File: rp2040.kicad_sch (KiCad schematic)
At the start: 15 parts, among them U3 RP2040

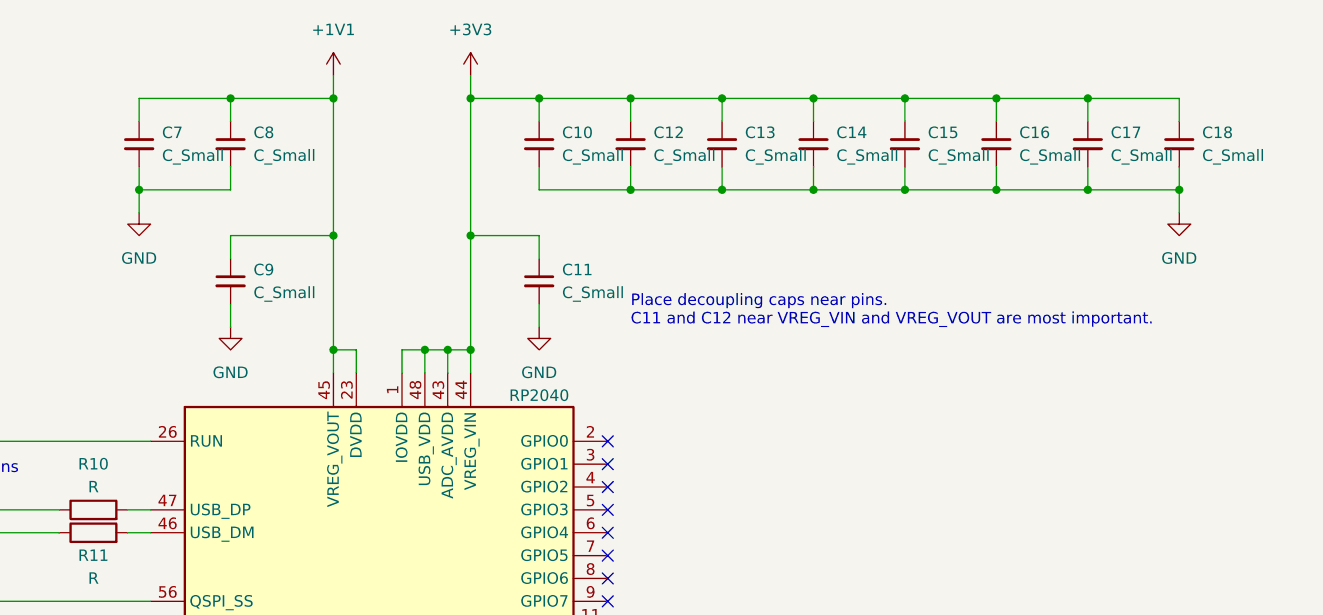
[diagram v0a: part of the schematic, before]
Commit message: Complete power regulator schematics
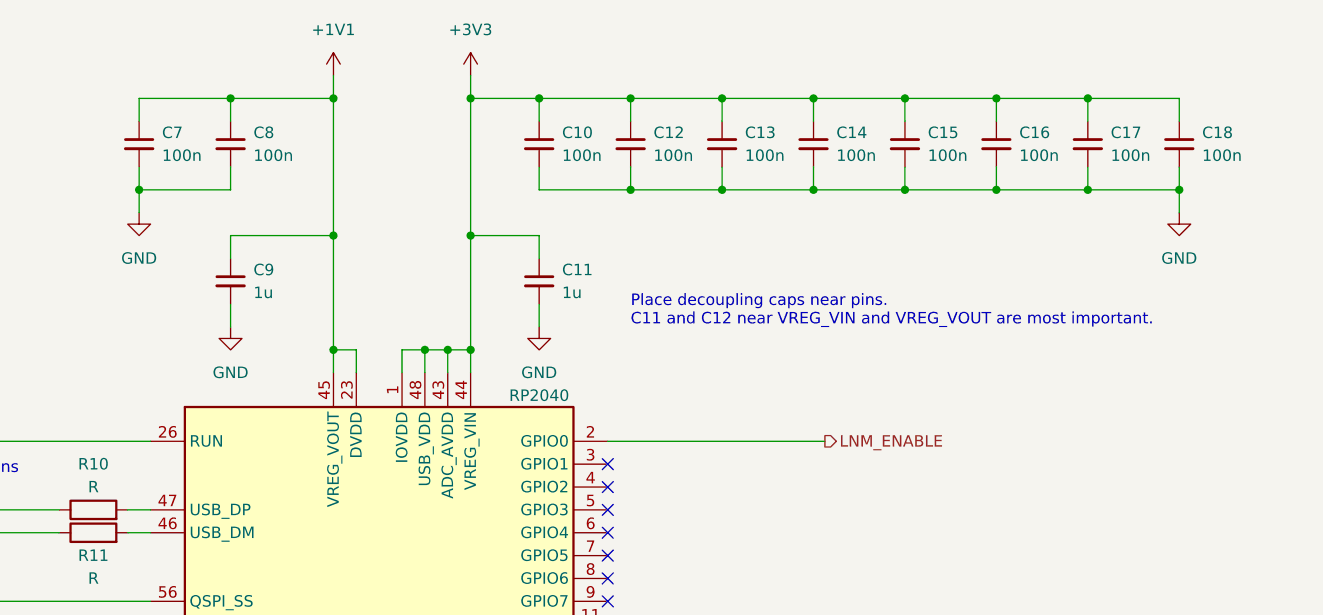
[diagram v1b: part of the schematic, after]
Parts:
- C10, C12, C13, C14, C15, C16, C17, C18, C7, C8: value C_Small -> 100n
- C11, C9: value C_Small -> 1u
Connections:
- net LNM_ENABLE: now reaches U3.2 (GPIO0)
- no-connect marks 30 -> 29
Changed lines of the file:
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@@
 		(at 166.37 115.57)
-	)
-	(no_connect
-		(at 166.37 72.39)
 	)
 	(bus_entry
@@
 		(pts
 			(xy 146.05 62.23) (xy 148.59 62.23)
+		)
+		(stroke
+			(width 0)
+			(type default)
+		)
+	)
+	(wire
+		(pts
+			(xy 166.37 72.39) (xy 190.5 72.39)
 		)
 		(stroke
@@
 			)
 			(justify right)
+		)
+	)
+	(hierarchical_label "LNM_ENABLE"
+		(shape output)
+		(at 190.5 72.39 0)
+		(fields_autoplaced yes)
+		(effects
+			(font
+				(size 1.27 1.27)
+			)
+			(justify left)
 		)
 	)
@@
 		(fields_autoplaced yes)
 		(property "Reference" "C13"
-			(at 181.61 38.1063 0)
+			(at 181.61 38.1062 0)
 			(effects
 				(font
@@
 			)
 		)
-		(property "Value" "C_Small"
-			(at 181.61 40.6463 0)
+		(property "Value" "100n"
+			(at 181.61 40.6462 0)
 			(effects
 				(font
@@
 		(fields_autoplaced yes)
 		(property "Reference" "C16"
-			(at 212.09 38.1063 0)
+			(at 212.09 38.1062 0)
 			(effects
 				(font
@@
 			)
 		)
-		(property "Value" "C_Small"
-			(at 212.09 40.6463 0)
+		(property "Value" "100n"
+			(at 212.09 40.6462 0)
 			(effects
 				(font
@@
 		(fields_autoplaced yes)
 		(property "Reference" "C14"
-			(at 191.77 38.1063 0)
+			(at 191.77 38.1062 0)
 			(effects
 				(font
@@
 			)
 		)
-		(property "Value" "C_Small"
-			(at 191.77 40.6463 0)
+		(property "Value" "100n"
+			(at 191.77 40.6462 0)
 			(effects
 				(font
@@
 		(fields_autoplaced yes)
 		(property "Reference" "C9"
-			(at 127 53.3463 0)
+			(at 127 53.3462 0)
 			(effects
 				(font
@@
 			)
 		)
-		(property "Value" "C_Small"
-			(at 127 55.8863 0)
+		(property "Value" "1u"
+			(at 127 55.8862 0)
 			(effects
 				(font
@@
 		(fields_autoplaced yes)
 		(property "Reference" "C7"
-			(at 116.84 38.1063 0)
+			(at 116.84 38.1062 0)
 			(effects
 				(font
@@
 			)
 		)
-		(property "Value" "C_Small"
-			(at 116.84 40.6463 0)
+		(property "Value" "100n"
+			(at 116.84 40.6462 0)
 			(effects
 				(font
@@
 		(fields_autoplaced yes)
 		(property "Reference" "C12"
-			(at 171.45 38.1063 0)
+			(at 171.45 38.1062 0)
 			(effects
 				(font
@@
 			)
 		)
-		(property "Value" "C_Small"
-			(at 171.45 40.6463 0)
+		(property "Value" "100n"
+			(at 171.45 40.6462 0)
 			(effects
 				(font
@@
 		(fields_autoplaced yes)
 		(property "Reference" "C11"
-			(at 161.29 53.3463 0)
+			(at 161.29 53.3462 0)
 			(effects
 				(font
@@
 			)
 		)
-		(property "Value" "C_Small"
-			(at 161.29 55.8863 0)
+		(property "Value" "1u"
+			(at 161.29 55.8862 0)
 			(effects
 				(font
@@
 		(fields_autoplaced yes)
 		(property "Reference" "C10"
-			(at 161.29 38.1063 0)
+			(at 161.29 38.1062 0)
 			(effects
 				(font
@@
 			)
 		)
-		(property "Value" "C_Small"
-			(at 161.29 40.6463 0)
+		(property "Value" "100n"
+			(at 161.29 40.6462 0)
 			(effects
 				(font
@@
 		(fields_autoplaced yes)
 		(property "Reference" "C17"
-			(at 222.25 38.1063 0)
+			(at 222.25 38.1062 0)
 			(effects
 				(font
@@
 			)
 		)
-		(property "Value" "C_Small"
-			(at 222.25 40.6463 0)
+		(property "Value" "100n"
+			(at 222.25 40.6462 0)
 			(effects
 				(font
@@
 		(fields_autoplaced yes)
 		(property "Reference" "C15"
-			(at 201.93 38.1063 0)
+			(at 201.93 38.1062 0)
 			(effects
 				(font
@@
 			)
 		)
-		(property "Value" "C_Small"
-			(at 201.93 40.6463 0)
+		(property "Value" "100n"
+			(at 201.93 40.6462 0)
 			(effects
 				(font
@@
 		(fields_autoplaced yes)
 		(property "Reference" "C18"
-			(at 232.41 38.1063 0)
+			(at 232.41 38.1062 0)
 			(effects
 				(font
@@
 			)
 		)
-		(property "Value" "C_Small"
-			(at 232.41 40.6463 0)
+		(property "Value" "100n"
+			(at 232.41 40.6462 0)
 			(effects
 				(font
@@
 		(fields_autoplaced yes)
 		(property "Reference" "C8"
-			(at 127 38.1063 0)
+			(at 127 38.1062 0)
 			(effects
 				(font
@@
 			)
 		)
-		(property "Value" "C_Small"
-			(at 127 40.6463 0)
-			(effects
-				(font
+		(property "Value" "100n"
+			(at 127 40.6462 0)
+			(effects
+				(font

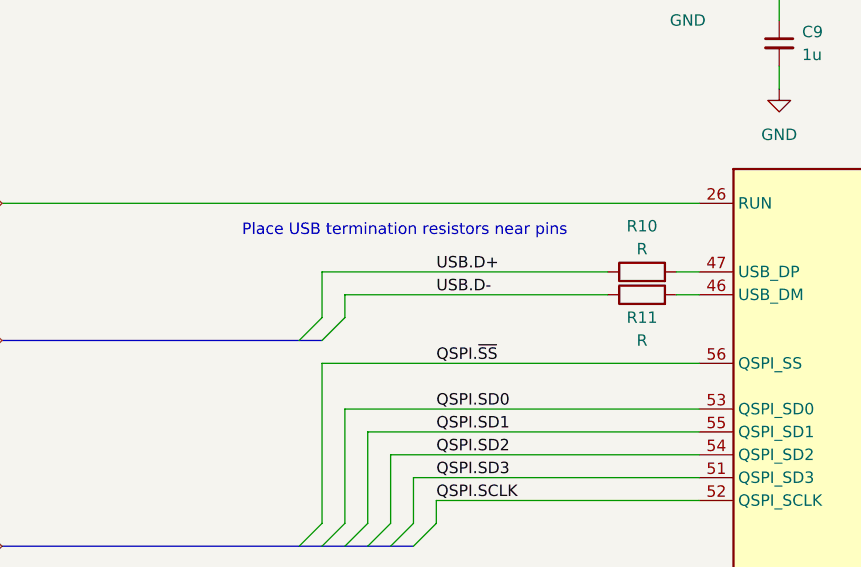
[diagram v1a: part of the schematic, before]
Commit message: Update footprints, route more circuit blocks
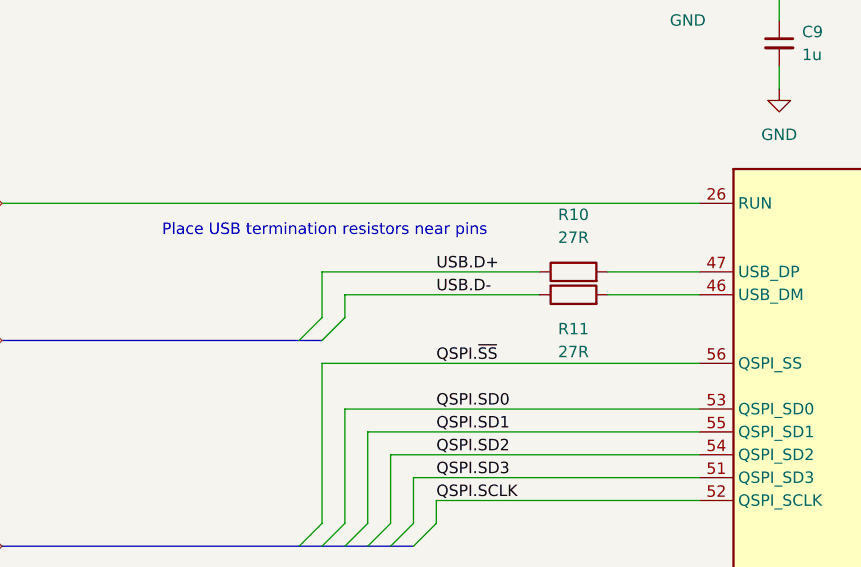
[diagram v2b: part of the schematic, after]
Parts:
- R10, R11: value R -> 27R
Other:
- moved on the sheet: R10, R11
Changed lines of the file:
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@@
 	(wire
 		(pts
-			(xy 76.2 82.55) (xy 105.41 82.55)
+			(xy 76.2 82.55) (xy 97.79 82.55)
 		)
 		(stroke
@@
 	(wire
 		(pts
-			(xy 113.03 80.01) (xy 115.57 80.01)
+			(xy 105.41 80.01) (xy 115.57 80.01)
 		)
 		(stroke
@@
 	(wire
 		(pts
-			(xy 113.03 82.55) (xy 115.57 82.55)
-		)
-		(stroke
-			(width 0)
-			(type default)
-		)
-	)
-	(wire
-		(pts
-			(xy 73.66 80.01) (xy 105.41 80.01)
+			(xy 105.41 82.55) (xy 115.57 82.55)
+		)
+		(stroke
+			(width 0)
+			(type default)
+		)
+	)
+	(wire
+		(pts
+			(xy 73.66 80.01) (xy 97.79 80.01)
 		)
 		(stroke
@@
 	(text "Place USB termination resistors near pins"
 		(exclude_from_sim no)
-		(at 64.77 76.2 0)
+		(at 55.88 76.2 0)
 		(effects
 			(font
@@
 	(symbol
 		(lib_id "Device:R")
-		(at 109.22 80.01 90)
+		(at 101.6 80.01 90)
 		(unit 1)
 		(exclude_from_sim no)
@@
 		(fields_autoplaced yes)
 		(property "Reference" "R10"
-			(at 109.22 74.93 90)
-			(effects
-				(font
-					(size 1.27 1.27)
-				)
-			)
-		)
-		(property "Value" "R"
-			(at 109.22 77.47 90)
+			(at 101.6 73.66 90)
+			(effects
+				(font
+					(size 1.27 1.27)
+				)
+			)
+		)
+		(property "Value" "27R"
+			(at 101.6 76.2 90)
 			(effects
 				(font
@@
 		)
 		(property "Footprint" "Resistor_SMD:R_0402_1005Metric"
-			(at 109.22 81.788 90)
+			(at 101.6 81.788 90)
 			(effects
 				(font
@@
 		)
 		(property "Datasheet" "~"
-			(at 109.22 80.01 0)
+			(at 101.6 80.01 0)
 			(effects
 				(font
@@
 		)
 		(property "Description" "Resistor"
-			(at 109.22 80.01 0)
+			(at 101.6 80.01 0)
 			(effects
 				(font
@@
 	(symbol
 		(lib_id "Device:R")
-		(at 109.22 82.55 90)
+		(at 101.6 82.55 90)
 		(unit 1)
 		(exclude_from_sim no)
@@
 		(fields_autoplaced yes)
 		(property "Reference" "R11"
-			(at 109.22 85.09 90)
-			(effects
-				(font
-					(size 1.27 1.27)
-				)
-			)
-		)
-		(property "Value" "R"
-			(at 109.22 87.63 90)
+			(at 101.6 86.36 90)
+			(effects
+				(font
+					(size 1.27 1.27)
+				)
+			)
+		)
+		(property "Value" "27R"
+			(at 101.6 88.9 90)
 			(effects
 				(font
@@
 		)
 		(property "Footprint" "Resistor_SMD:R_0402_1005Metric"
-			(at 109.22 84.328 90)
+			(at 101.6 84.328 90)
 			(effects
 				(font
@@
 		)
 		(property "Datasheet" "~"
-			(at 109.22 82.55 0)
+			(at 101.6 82.55 0)
 			(effects
 				(font
@@
 		)
 		(property "Description" "Resistor"
-			(at 109.22 82.55 0)
-			(effects
-				(font
+			(at 101.6 82.55 0)
+			(effects
+				(font

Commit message: Big update, bad commit messsage :)
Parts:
- added R503: 0R, cubesat_rp2040:R_0402_1005Metric, symbol Device:R
- C501: renamed from C7; footprint Capacitor_SMD:C_0402_1005Metric -> cubesat_rp2040:C_0402_1005Metric
- C502: renamed from C8; footprint Capacitor_SMD:C_0402_1005Metric -> cubesat_rp2040:C_0402_1005Metric
- C503: renamed from C9; footprint Capacitor_SMD:C_0402_1005Metric -> cubesat_rp2040:C_0402_1005Metric
- C504: renamed from C10; footprint Capacitor_SMD:C_0402_1005Metric -> cubesat_rp2040:C_0402_1005Metric
- C505: renamed from C11; footprint Capacitor_SMD:C_0402_1005Metric -> cubesat_rp2040:C_0402_1005Metric
- C506: renamed from C12; footprint Capacitor_SMD:C_0402_1005Metric -> cubesat_rp2040:C_0402_1005Metric
- C507: renamed from C13; footprint Capacitor_SMD:C_0402_1005Metric -> cubesat_rp2040:C_0402_1005Metric
- C508: renamed from C14; footprint Capacitor_SMD:C_0402_1005Metric -> cubesat_rp2040:C_0402_1005Metric
- C509: renamed from C15; footprint Capacitor_SMD:C_0402_1005Metric -> cubesat_rp2040:C_0402_1005Metric
- C510: renamed from C16; footprint Capacitor_SMD:C_0402_1005Metric -> cubesat_rp2040:C_0402_1005Metric
- C511: renamed from C17; footprint Capacitor_SMD:C_0402_1005Metric -> cubesat_rp2040:C_0402_1005Metric
- C512: renamed from C18; footprint Capacitor_SMD:C_0402_1005Metric -> cubesat_rp2040:C_0402_1005Metric
- R501: renamed from R10; footprint Resistor_SMD:R_0402_1005Metric -> cubesat_rp2040:R_0402_1005Metric
- R502: renamed from R11; footprint Resistor_SMD:R_0402_1005Metric -> cubesat_rp2040:R_0402_1005Metric
- renumbered U3 to U501
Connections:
- net GND: now also R503.1; no longer U501.19 (TESTEN)
- net ADC0: now reaches U501.38 (GPIO26_ADC0)
- net ADC1: now reaches U501.39 (GPIO27_ADC1)
- net ADC2: now reaches U501.40 (GPIO28_ADC2)
- net ADC3: now reaches U501.41 (GPIO29_ADC3)
- net SWDCLK renamed SWCLK
- net XOUT: no longer names the net of U501.21 (XOUT)
- new net: R503.2, U501.19 (TESTEN)
- no-connect marks 29 -> 30
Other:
- note added: "RP2040 requires 27R termination resistors near pins. R_{pu} and R_{pd} are internal and configurable."
- note removed: "Place USB termination resistors near pins"
- company: (none) -> Magnus Oksbøl Therkelsen
- title: (none) -> CubeSat RP2040 Board

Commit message: Major update, everything has been touched
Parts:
- added C501: 100n, cubesat_rp2040:C_0402_1005Metric, symbol Device:C
- added C506, C515: 100n, cubesat_rp2040:C_0402_1005Metric, symbol Device:C_Small
- added J501: FTSH-105-01-L-DV-007, cubesat_rp2040:SAMTEC_FTSH-105-01-L-DV-007, symbol cubesat_rp2040:CoreSight_10_Conn
- added R502: 0R, cubesat_rp2040:R_0402_1005Metric, symbol Device:R
- added R505, R506, R507: 100k, cubesat_rp2040:R_0402_1005Metric, symbol Device:R
- added R510: 1k, cubesat_rp2040:R_0402_1005Metric, symbol Device:R
- added U503: S25FL128SAGNFM000, cubesat_rp2040:SON8_S25FL128SAGNFI001_INF, symbol cubesat_rp2040:S25FL128S
- R501: renamed from R503; MANUFACTURER (none) -> Vishay; Manufacturer_Name (none) -> Vishay; Manufacturer_Part_Number (none) -> P-0402ExxxxFGxx; now not fitted
- R508: renamed from R501; MANUFACTURER (none) -> Vishay; Manufacturer_Name (none) -> Vishay; Manufacturer_Part_Number (none) -> P-0402E27R0FGxx
- R509: renamed from R502; MANUFACTURER (none) -> Vishay; Manufacturer_Name (none) -> Vishay; Manufacturer_Part_Number (none) -> P-0402E27R0FGxx
- U502: renamed from U501; Manufacturer_Part_Number (none) -> RP2040
- renumbered C503 to C502, C505 to C503, C501 to C504, C502 to C505, C504 to C507, C506 to C508, C507 to C509, C508 to C510, C509 to C511, C510 to C512, C511 to C513, C512 to C514
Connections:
- net +1V1: now also C506.1
- net +3V3: now also R501.2, C501.1, C515.1, J501.01 (VTREF), R505.2, R507.2, U503.8 (VCC)
- net ADC0: no longer U502.38 (GPIO26_ADC0)
- net ADC1: no longer U502.39 (GPIO27_ADC1)
- net ADC2: no longer U502.40 (GPIO28_ADC2)
- net ADC3: no longer U502.41 (GPIO29_ADC3)
- net GND: now also C501.2, C506.2, C515.2, J501.03 (GND), J501.05 (GND), J501.09 (GND), R502.2, R506.1, U503.4 (VSS), U503.9 (EP); no longer R501.1
- net LNM_ENABLE: now also U502.40 (GPIO28_ADC2); no longer U502.2 (GPIO0)
- net QSPI.SCLK: now also U503.6 (SCK)
- net QSPI.SD0: now also U503.5 (SI/IO0)
- net QSPI.SD1: now also U503.2 (SO/IO1)
- net QSPI.SD2: now also U503.3 (~{WP}/IO2)
- net QSPI.SD3: now also U503.7 (~{HOLD}/IO3)
- net QSPI.~{SS}: now also R510.1, U503.1 (~{CS})
- net RUN: now also J501.10 (nSRST), R507.1
- net SWCLK: now also J501.04 (TCK/SWCLK), R506.2
- net SWDIO: now also J501.02 (TMS/SWDIO), R505.1
- net TESTEN: now reaches U502.19 (TESTEN)
- net TESTEN: now also R501.1, R502.1; no longer R501.2
- net D+: now reaches R508.2, U502.47 (USB_DP)
- net GPIO8: now reaches U502.11 (GPIO8)
- net GPIO9: now reaches U502.12 (GPIO9)
- net GPIO10: now reaches U502.13 (GPIO10)
- net GPIO11: now reaches U502.14 (GPIO11)
- net GPIO12: now reaches U502.15 (GPIO12)
- net GPIO13: now reaches U502.16 (GPIO13)
- net GPIO14: now reaches U502.17 (GPIO14)
- net GPIO15: now reaches U502.18 (GPIO15)
- net GPIO16: now reaches U502.27 (GPIO16)
- net GPIO17: now reaches U502.28 (GPIO17)
- net GPIO18: now reaches U502.29 (GPIO18)
- net GPIO1: now reaches U502.3 (GPIO1)
- net GPIO19: now reaches U502.30 (GPIO19)
- net GPIO20: now reaches U502.31 (GPIO20)
- net GPIO21: now reaches U502.32 (GPIO21)
- net GPIO22: now reaches U502.34 (GPIO22)
- net GPIO23: now reaches U502.35 (GPIO23)
- net GPIO24: now reaches U502.36 (GPIO24)
- net GPIO25: now reaches U502.37 (GPIO25)
- net GPIO2: now reaches U502.4 (GPIO2)
- net D-: now reaches R509.2, U502.46 (USB_DM)
- net GPIO3: now reaches U502.5 (GPIO3)
- net GPIO4: now reaches U502.6 (GPIO4)
- net GPIO5: now reaches U502.7 (GPIO5)
- net GPIO6: now reaches U502.8 (GPIO6)
- net GPIO7: now reaches U502.9 (GPIO7)
- net XIN renamed 48M0_CLK
- new net GPIO0: U502.2 (GPIO0)
- new net GPIO26/ADC0: U502.38 (GPIO26_ADC0)
- new net GPIO27/ADC1: U502.39 (GPIO27_ADC1)
- new net USB_VBUS_DET: U502.41 (GPIO29_ADC3)
- new net ~{USB_BOOT}: R510.2
- no-connect marks 30 -> 31
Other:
- note added: "ARM Coresight 10 compatible pinout. Only SWD, nSRST and VTref exposed."
- note added: "Place decoupling caps near VCC"
- note added: "Place decoupling caps near pins. VREG_VIN and VREG_VOUT are most important."
- note removed: "Place decoupling caps near pins. C11 and C12 near VREG_VIN and VREG_VOUT are most important."
- moved on the sheet: C502, C503, C504, C505, C507, C508, C509, C510, C511, C512, C513, C514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
